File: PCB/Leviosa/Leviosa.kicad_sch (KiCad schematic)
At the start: 35 parts, among them J1 Conn_01x03, J2 Conn_01x03, J3 Conn_01x04, Q3 TIP122, Q4 TIP122, U1 LM324, U2 ATtiny13A-P, U3 TPS1H200AQDGNRQ1, U5 L7805, U6 SS495A

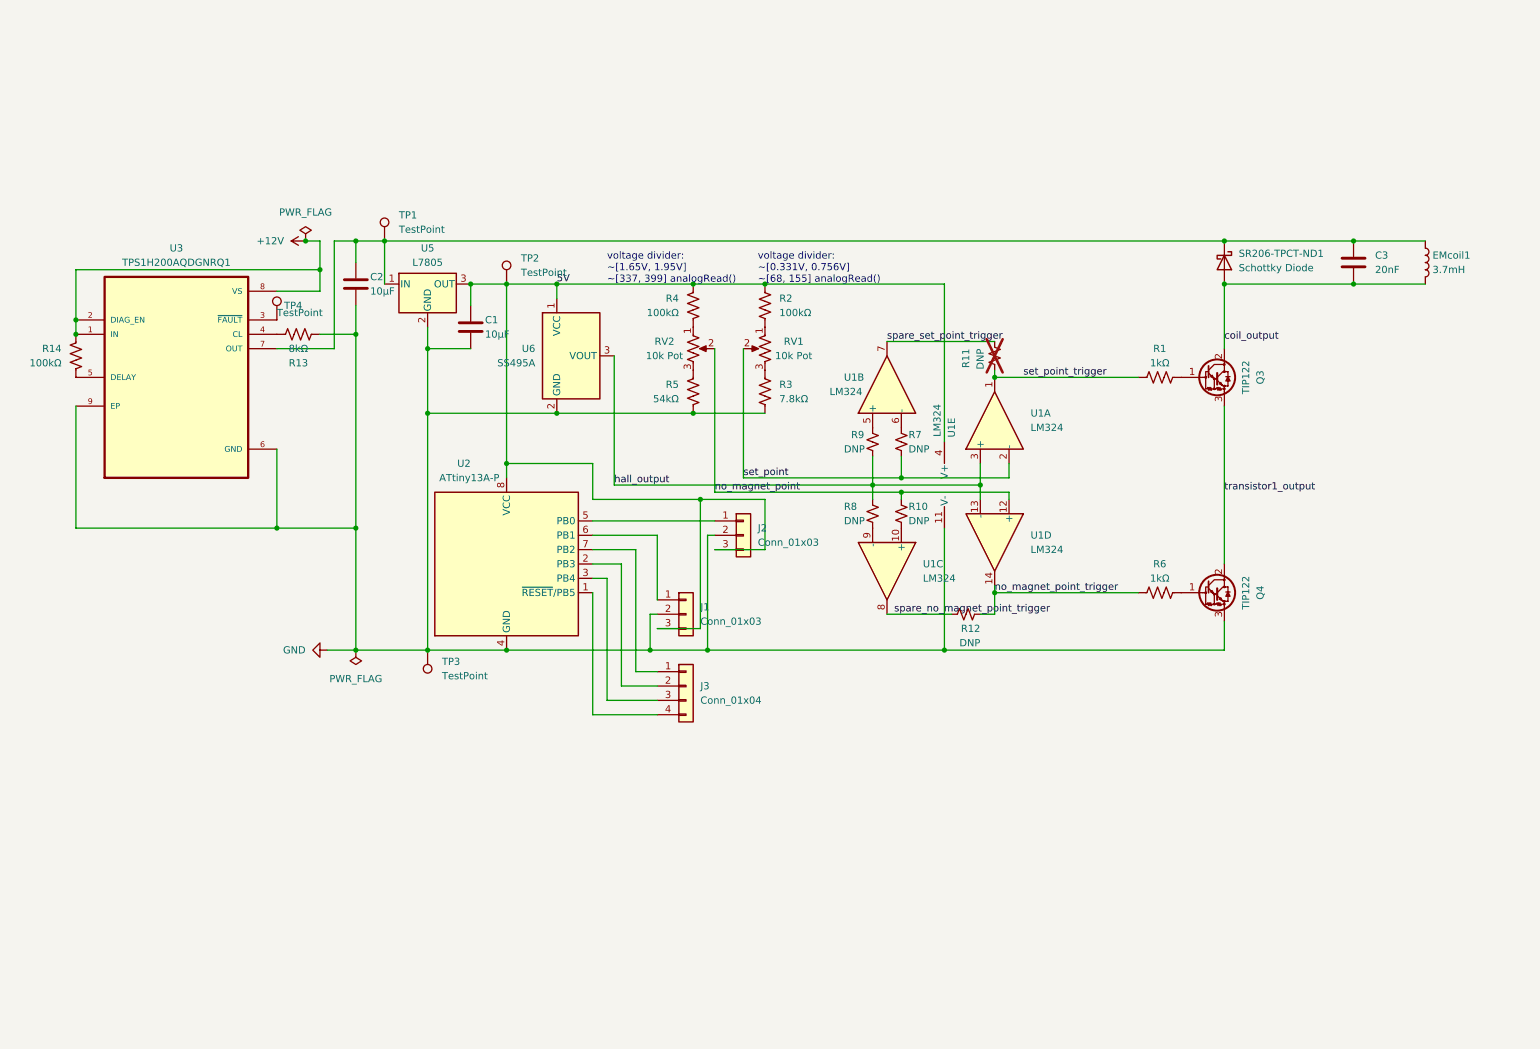
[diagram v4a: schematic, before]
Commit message: update schematic and swap DNP resistors for jumper pads
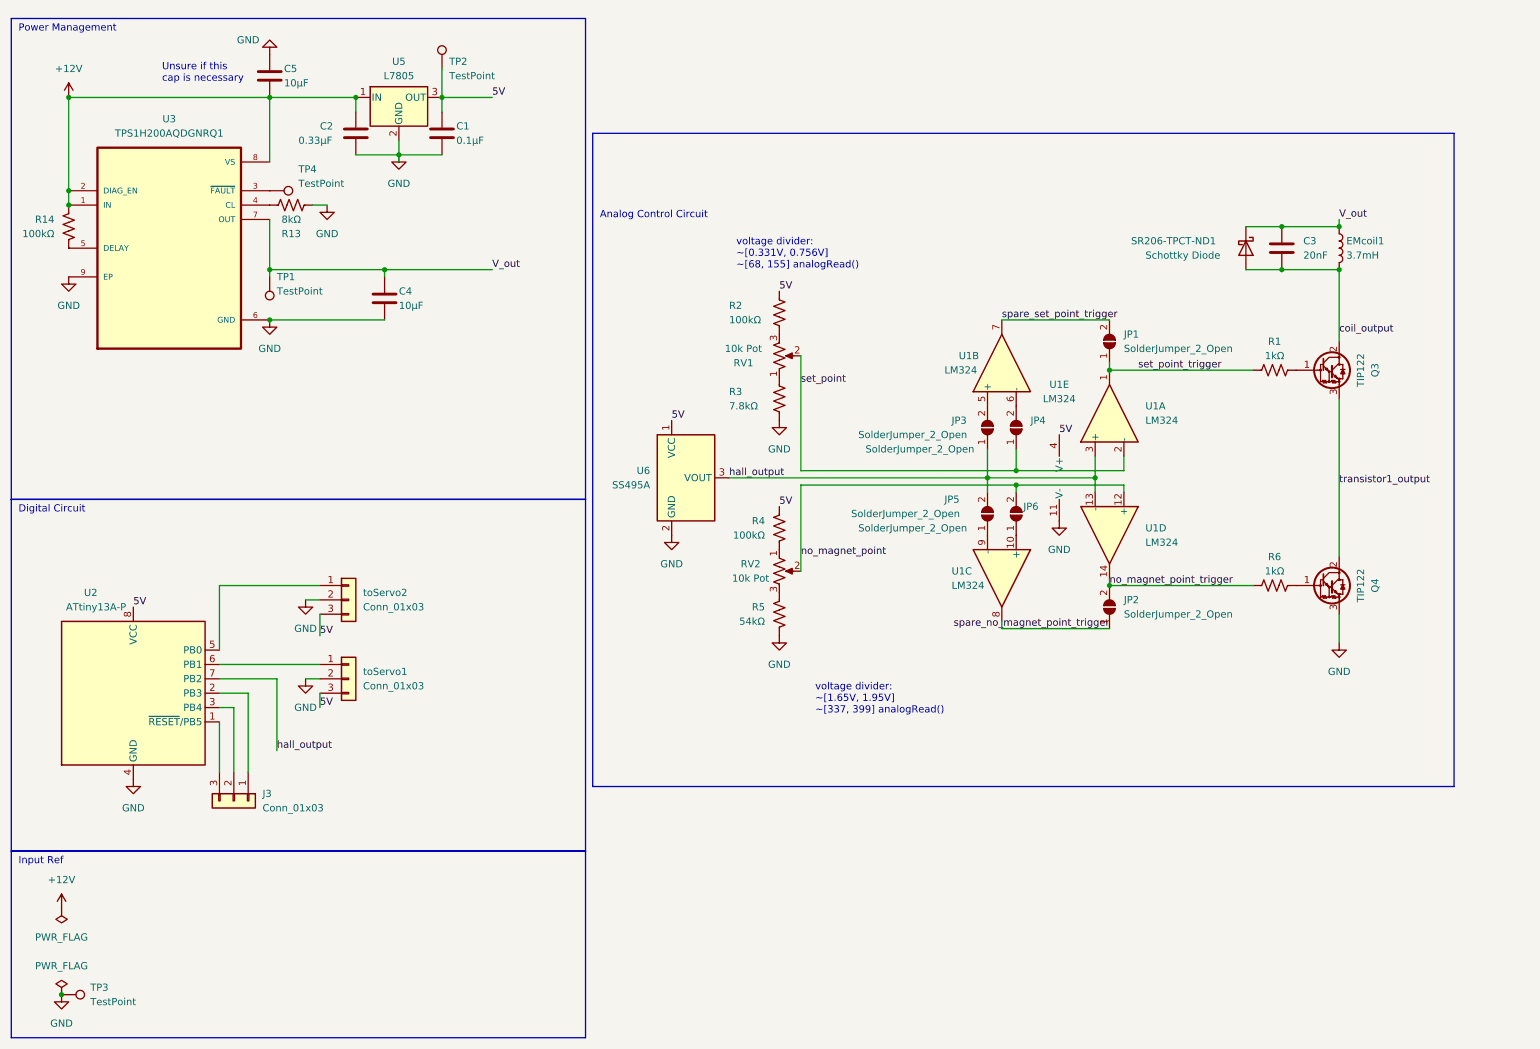
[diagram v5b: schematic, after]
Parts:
- removed J3: Conn_01x04, symbol Connector_Generic:Conn_01x04
- removed R10, R11, R12, R7, R8, R9: DNP, Resistor_SMD:R_0402_1005Metric_Pad0.72x0.64mm_HandSolder, symbol Device:R_Small_US
- added C4, C5: 10µF, Capacitor_THT:CP_Axial_L10.0mm_D6.0mm_P15.00mm_Horizontal, symbol Device:C
- added J3: Conn_01x03, symbol Connector_Generic:Conn_01x03
- added JP1, JP2, JP3, JP4, JP5, JP6: SolderJumper_2_Open, Jumper:SolderJumper-2_P1.3mm_Open_Pad1.0x1.5mm, symbol Jumper:SolderJumper_2_Open
- C1: value 10µF -> 0.1µF
- C2: value 10µF -> 0.33µF
- renumbered J1 to toServo1, J2 to toServo2
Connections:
- net +12V: now also C2.1, U5.1 (IN), C5.2
- net GND: now also C4.2, C5.1
- net hall_output: now also U2.7 (PB2), JP3.1 (A), JP5.2 (B)
- net no_magnet_point: now also JP6.2 (B)
- net no_magnet_point_trigger: now also JP2.2 (B)
- net set_point: now also JP4.1 (A)
- net set_point_trigger: now also JP1.1 (A)
- net spare_no_magnet_point_trigger: now also JP2.1 (A)
- net spare_set_point_trigger: now also JP1.2 (B)
- net at U2.2 (PB3): now also J3.1 (Pin_1)
- net at U2.3 (PB4): now also J3.2 (Pin_2)
- net at U2.1 (~{RESET}/PB5): now also J3.3 (Pin_3)
- net V_out: now reaches C3.1, EMcoil1.1, SR206-TPCT-ND1.1 (K), TP1.1, U3.7 (OUT)
- net V_out: now also C4.1; no longer C2.1, U5.1 (IN)
- net at U1.5 (+): now also JP3.2 (B)
- net at U1.6 (-): now also JP4.2 (B)
- net at R3.2: now also RV1.1; no longer RV1.3
- net at U1.10 (+): now also JP6.1 (A)
- net at U1.9 (-): now also JP5.1 (A)
- net at R2.1: now also RV1.3; no longer RV1.1
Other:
- note added: "Analog Control Circuit"
- note added: "Digital Circuit"
- note added: "Input Ref"
- note added: "Power Management"
- note added: "Unsure if this cap is necessary"
- moved on the sheet: C1, C2, C3, EMcoil1, Q3, Q4, R1, R13, R14, R2, R3, R4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

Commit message: add LED status lights and alter some footprints
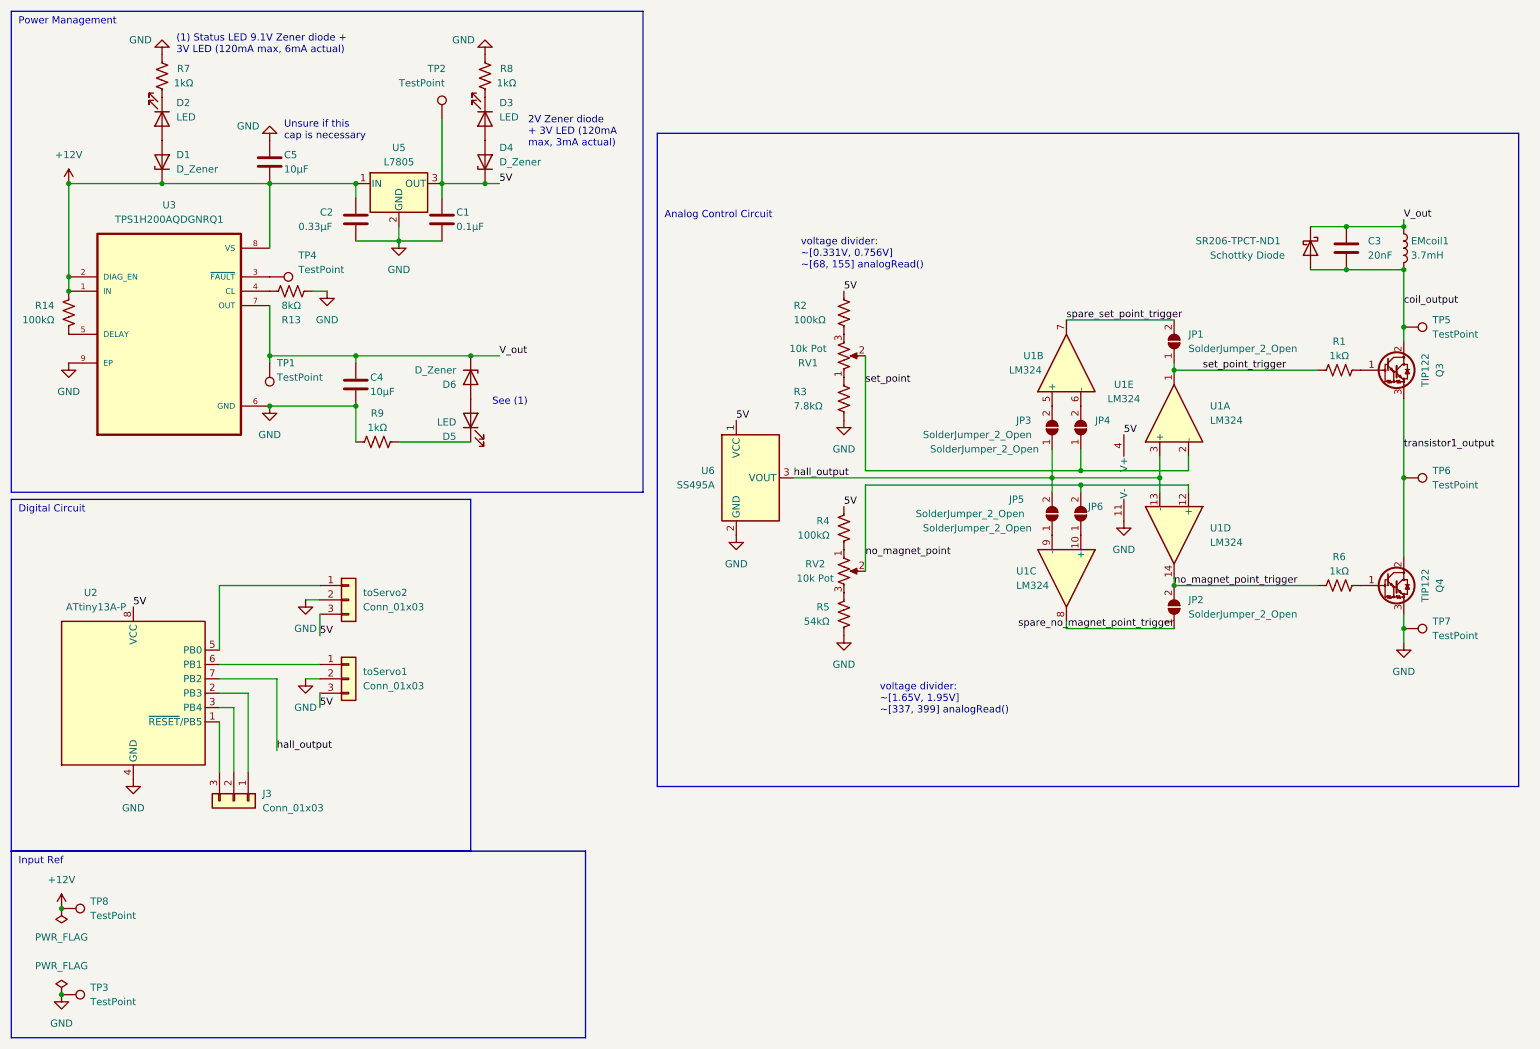
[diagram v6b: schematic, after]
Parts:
- added D1, D4, D6: D_Zener, symbol Device:D_Zener
- added D2, D3, D5: LED, symbol Device:LED
- added R7, R8, R9: 1kΩ, Resistor_SMD:R_0402_1005Metric_Pad0.72x0.64mm_HandSolder, symbol Device:R_US
- added TP5, TP6, TP7, TP8: TestPoint, TestPoint:TestPoint_Pad_D3.0mm, symbol Connector:TestPoint
- R1, R13, R14, R2, R3, R4, R5, R6: footprint Resistor_THT:R_Axial_DIN0411_L9.9mm_D3.6mm_P12.70mm_Horizontal -> Resistor_SMD:R_0402_1005Metric_Pad0.72x0.64mm_HandSolder
- TP1, TP2, TP3, TP4: footprint (none) -> TestPoint:TestPoint_Pad_D3.0mm
- U3: AVAILABILITY In Stock -> (none); CHECK_PRICES https://www.snapeda.com/parts/TPS1H200AQDGNRQ1/Texas+Instru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 -> (none); DESCRIPTION 40-V, 200-mΩ, 1-ch automotive smart high-side switch with a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 -> (none); MF Texas Instruments -> (none); MP TPS1H200AQDGNRQ1 -> (none); PACKAGE HVSSOP-8 Texas Instruments -> (none); PRICE None -> (none); PURCHASE-URL https://www.snapeda.com/api/url_track_click_mouser/?unipart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 -> (none); SNAPEDA_LINK https://www.snapeda.com/parts/TPS1H200AQDGNRQ1/Texas+Instru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 -> (none)
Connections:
- net +12V: now also D1.1 (K), TP8.1
- net 5V: now also D4.1 (K)
- net GND: now also R7.2, R8.2, R9.2, TP7.1
- net V_out: now also D6.1 (K)
- net coil_output: now also TP5.1
- net transistor1_output: now also TP6.1
- new net: D5.2 (A), D6.2 (A)
- new net: D2.1 (K), R7.1
- new net: D5.1 (K), R9.1
- new net: D3.2 (A), D4.2 (A)
- new net: D3.1 (K), R8.1
- new net: D1.2 (A), D2.2 (A)
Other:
- note added: "(1) Status LED 9.1V Zener diode + 3V LED (120mA max, 6mA actual)"
- note added: "2V Zener diode + 3V LED (120mA max, 3mA actual)"
- note added: "See (1)"
- moved on the sheet: C1, C2, C3, C4, C5, EMcoil1, JP1, JP2, JP3, JP4, JP5, JP6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

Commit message: update schematic footprints. PCB is sad now
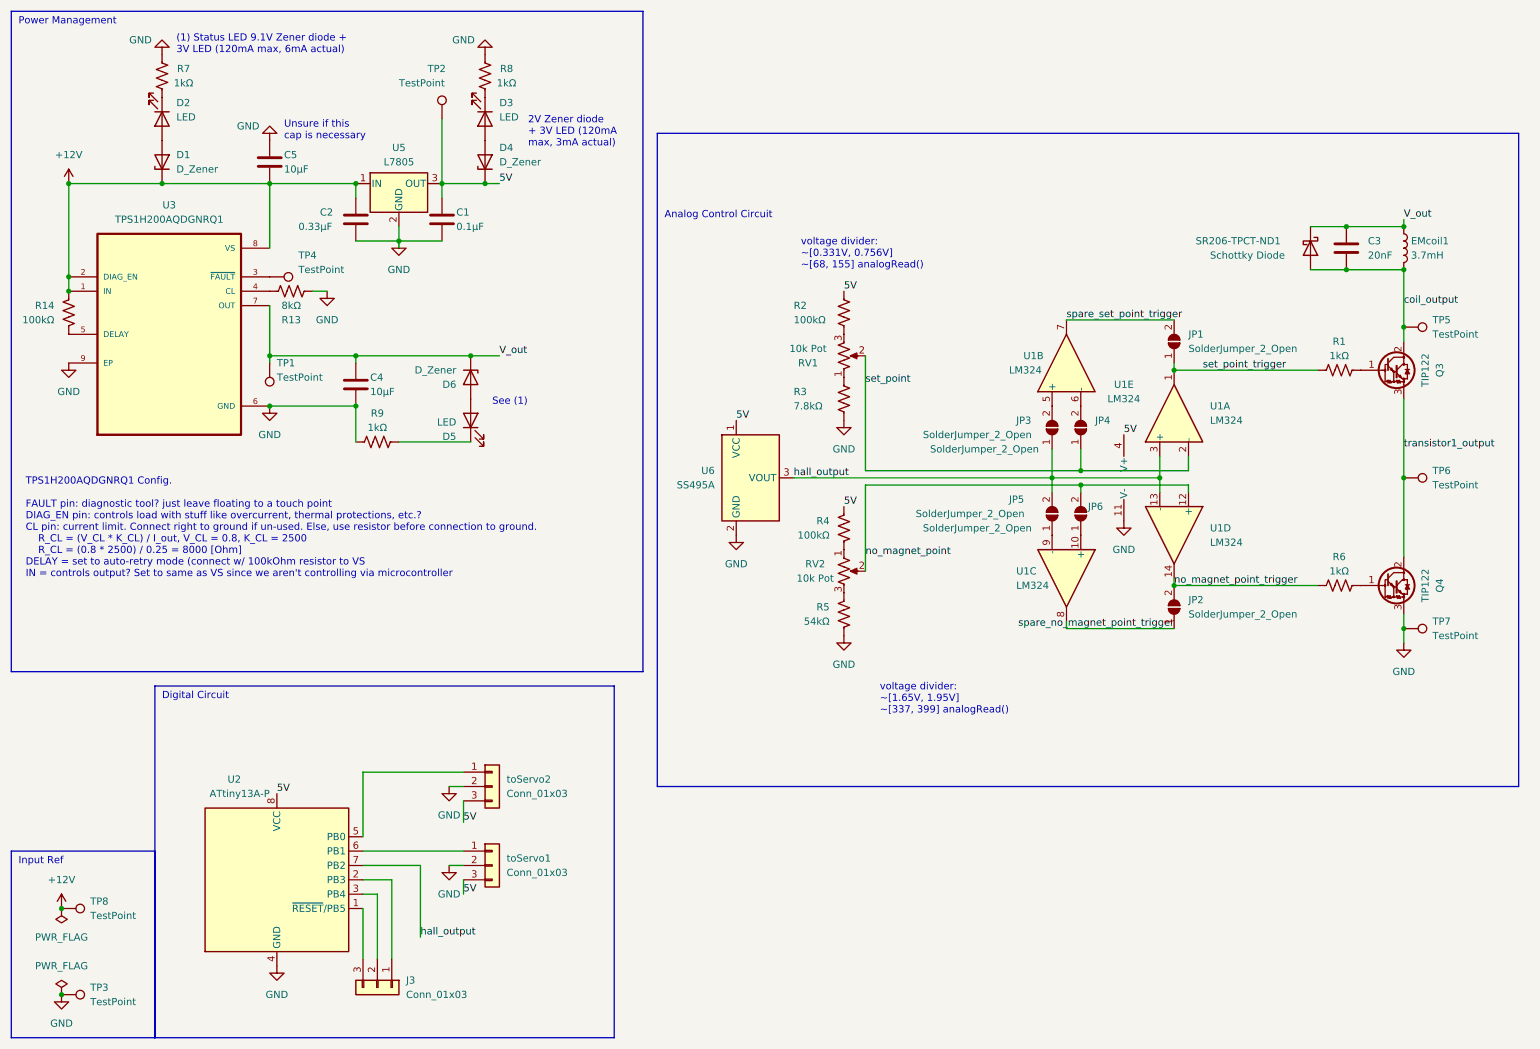
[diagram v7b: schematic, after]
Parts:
- D1, D6: footprint (none) -> SMAZ9V1-13-F:SMA_DIO
- D2, D3, D5: footprint (none) -> MP-2016-1100-50-70:LED_MP-2016-1100-50-70
- D4: footprint (none) -> SZMMSZ4679T1G:SOD-123_ONS
- J3, toServo1, toServo2: footprint (none) -> Connector_JST:JST_ACH_BM03B-ACHSS-GAN-ETF_1x03-1MP_P1.20mm_Vertical
- U1: footprint (none) -> Package_DIP:DIP-14_W7.62mm
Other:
- note added: "TPS1H200AQDGNRQ1 Config. FAULT pin: diagnostic tool? just leave floating to a touch point DIAG_EN pin: controls load with stuff like overcurrent, thermal protections, etc.? CL pin: current limit. Connect right to ground if un-used. Else, use resistor before connection to ground. R_CL = (V_CL * K_CL) / I_out, V_CL = 0.8, K_CL = 2500 R_CL = (0.8 * 2500) / 0.25 = 8000 [Ohm] DELAY = set to auto-retry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"
- moved on the sheet: J3, U2, toServo1, toServo2
